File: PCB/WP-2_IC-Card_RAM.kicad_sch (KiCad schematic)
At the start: 8 parts, among them J1 Conn_01x38_Female, U1 628128_TSOP

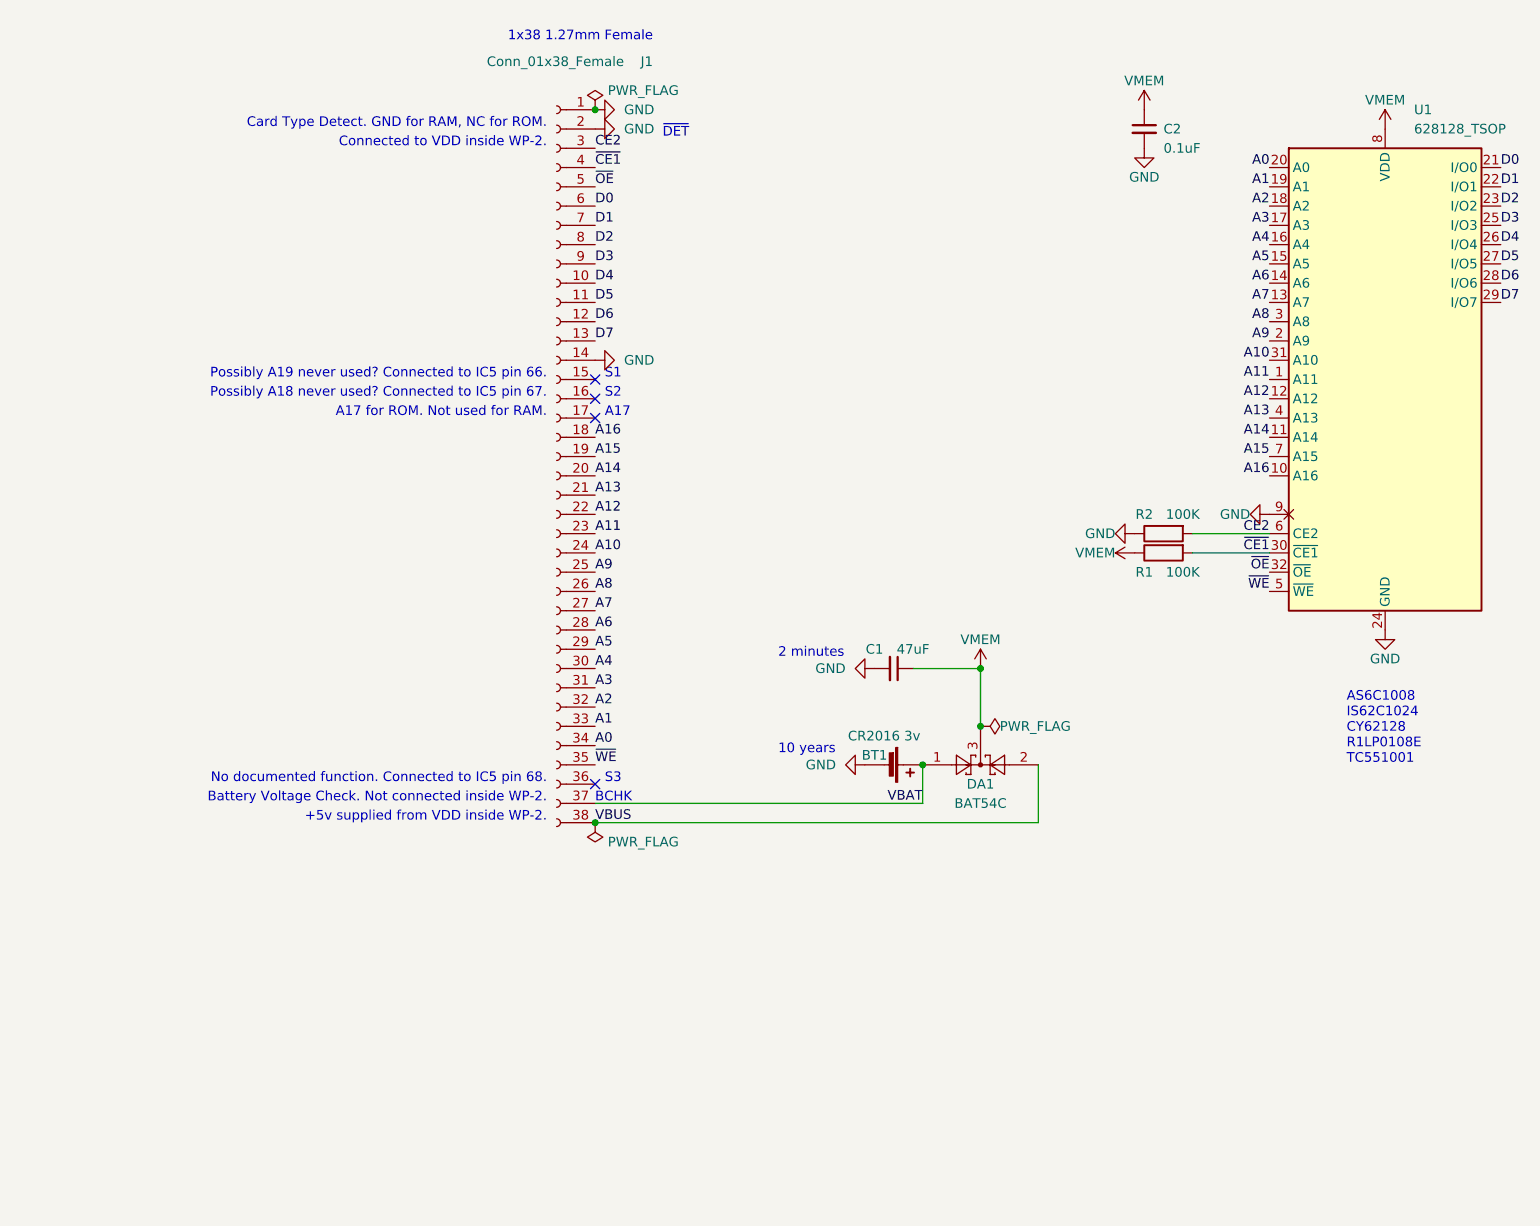
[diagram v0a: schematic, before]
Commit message: simpler caps for ram card, 3d-printed cover, new WIP 4-bank MRAM card
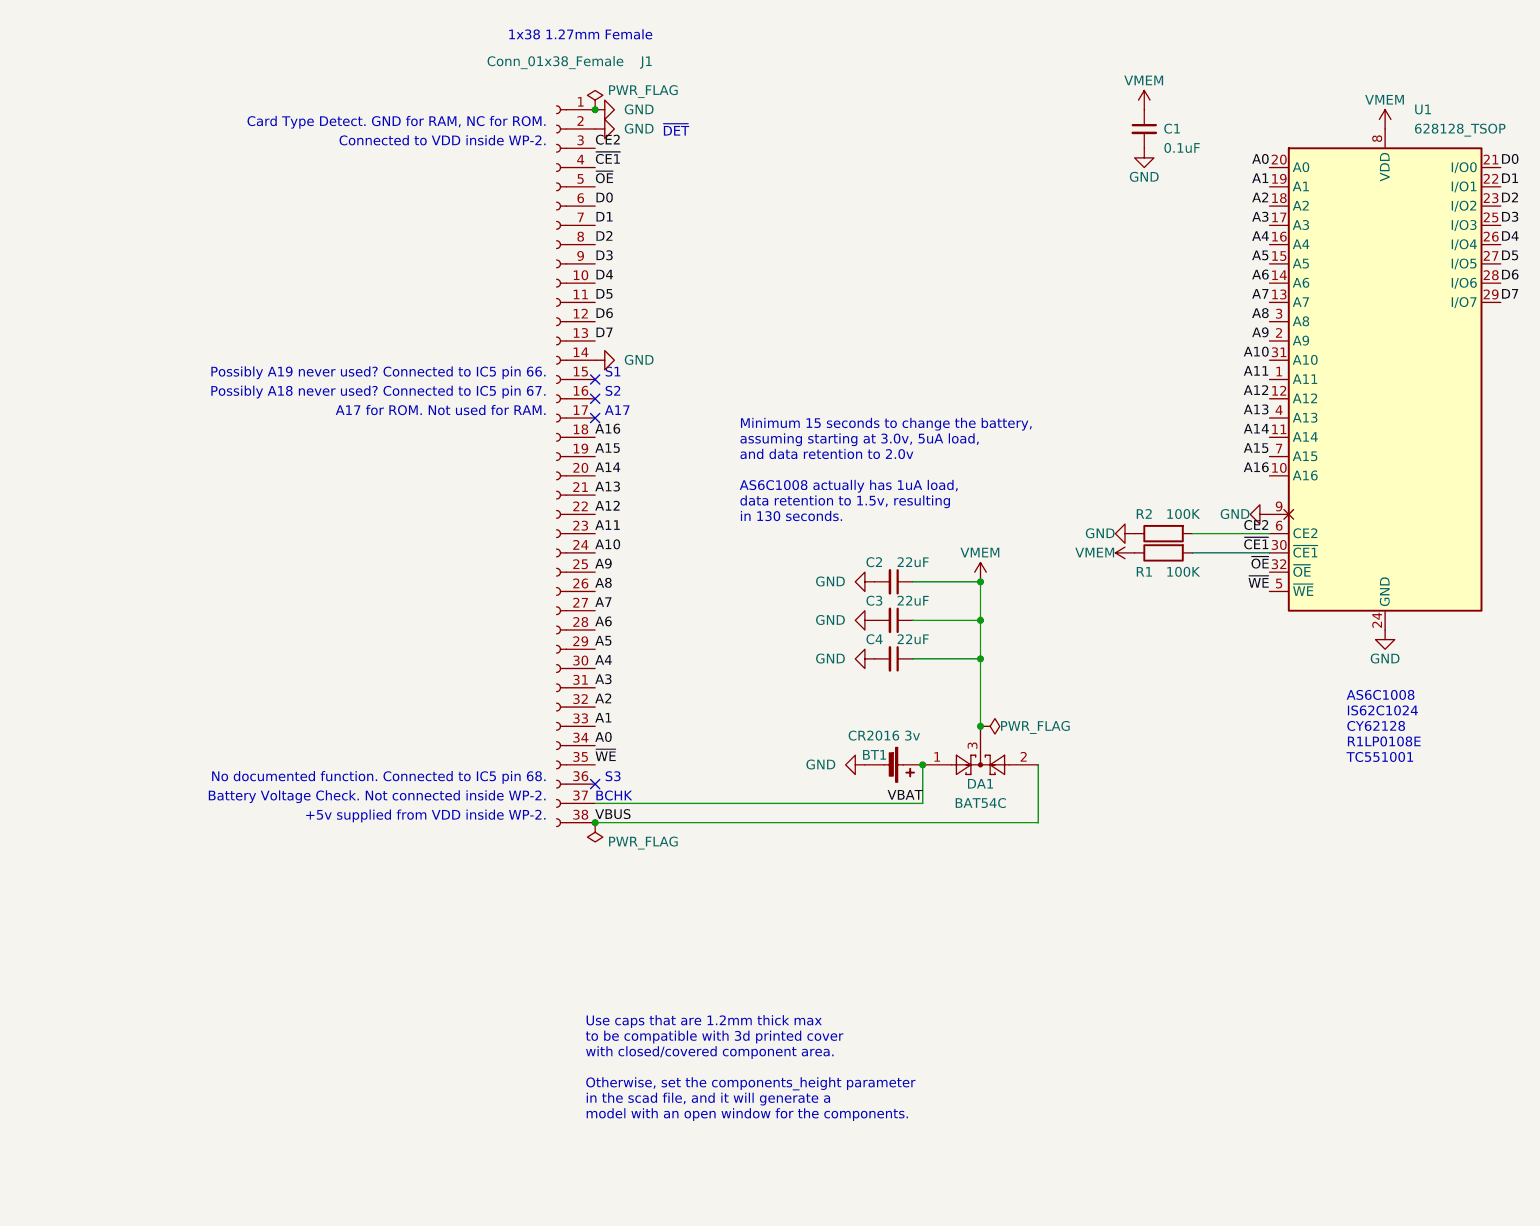
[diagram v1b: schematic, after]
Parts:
- added C3, C4: 22uF, 0_LOCAL:C_0805_1mm, symbol 0_LOCAL:C_Small
- C1: renamed from C2; footprint 0_LOCAL:C_0805 -> 0_LOCAL:C_0805_1mm
- C2: renamed from C1; value 47uF -> 22uF; footprint 0_LOCAL:C_0805 -> 0_LOCAL:C_0805_1mm
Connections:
- net GND: now also C3.2, C4.2
- net VMEM: now also C3.1, C4.1
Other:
- note added: "Minimum 15 seconds to change the battery, assuming starting at 3.0v, 5uA load, and data retention to 2.0v AS6C1008 actually has 1uA load, data retention to 1.5v, resulting in 130 seconds."
- note added: "Use caps that are 1.2mm thick max to be compatible with 3d printed cover with closed/covered component area. Otherwise, set the components_height parameter in the scad file, and it will generate a model with an open window for the components."
- note removed: "10 years"
- note removed: "2 minutes"
- moved on the sheet: C2

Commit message: readme
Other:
- note added: "Minimum 15 seconds to change the battery, assuming starting at 3.0v, 5uA load, and data retention to 2.0v AS6C1008 actually has 1uA load, data retention to 1.5v, resulting in 130 seconds. Actually tested over 10 minutes with no battery."
- note added: "The CE2 and BCHK circuits are included here even though they are no-op in the WP-2. Maybe the card might also work in other machines like the Citizen, and maybe some other machine actually uses those pins."
- note removed: "Minimum 15 seconds to change the battery, assuming starting at 3.0v, 5uA load, and data retention to 2.0v AS6C1008 actually has 1uA load, data retention to 1.5v, resulting in 130 seconds."
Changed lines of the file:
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@@
+    (effects (font (size 1.27 1.27)) (justify left bottom))
+  )
+  (text "The CE2 and BCHK circuits are included here even though they are no-op in the WP-2.\nMaybe the card might also work in other machines like the Citizen,\nand maybe some other machine actually uses those pins."
+    (at 44.45 198.12 0)
     (effects (font (size 1.27 1.27)) (justify left bottom))
   )
@@
     (effects (font (size 1.27 1.27)) (justify right bottom))
   )
-  (text "Minimum 15 seconds to change the battery,\nassuming starting at 3.0v, 5uA load,\nand data retention to 2.0v\n\nAS6C1008 actually has 1uA load,\ndata retention to 1.5v, resulting\nin 130 seconds."
-    (at 107.95 107.95 0)
+  (text "Minimum 15 seconds to change the battery,\nassuming starting at 3.0v, 5uA load,\nand data retention to 2.0v\n\nAS6C1008 actually has 1uA load,\ndata retention to 1.5v, resulting\nin 130 seconds.\n\nActually tested over 10 minutes with no battery."
+    (at 107.95 104.14 0)
     (effects (font (size 1.27 1.27)) (justify left bottom))
   )
@@
   )
   (text "Use caps that are 1.2mm thick max\nto be compatible with 3d printed cover\nwith closed/covered component area.\n\nOtherwise, set the components_height parameter\nin the scad file, and it will generate a\nmodel with an open window for the components.\n"
-    (at 87.63 186.69 0)
+    (at 44.45 185.42 0)
     (effects (font (size 1.27 1.27)) (justify left bottom))
   )

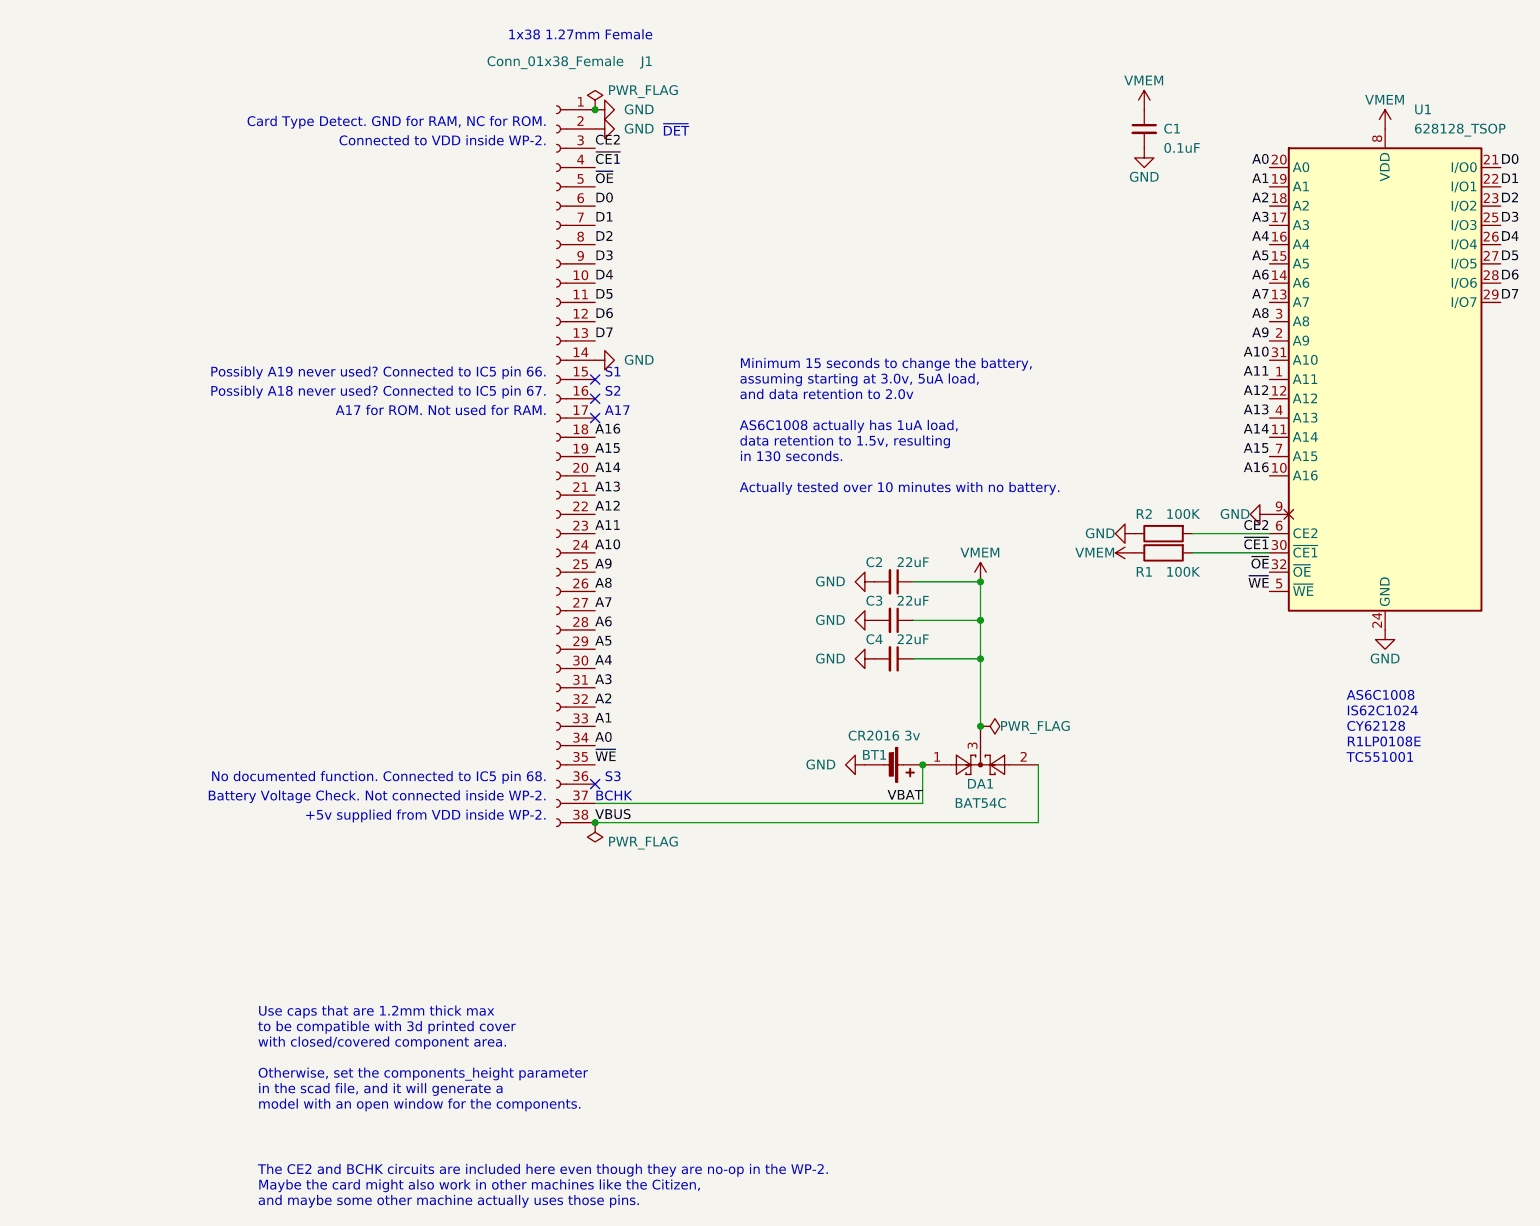
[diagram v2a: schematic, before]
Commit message: MRAM level shifters, delete FRAM, local datasheets in local symbols
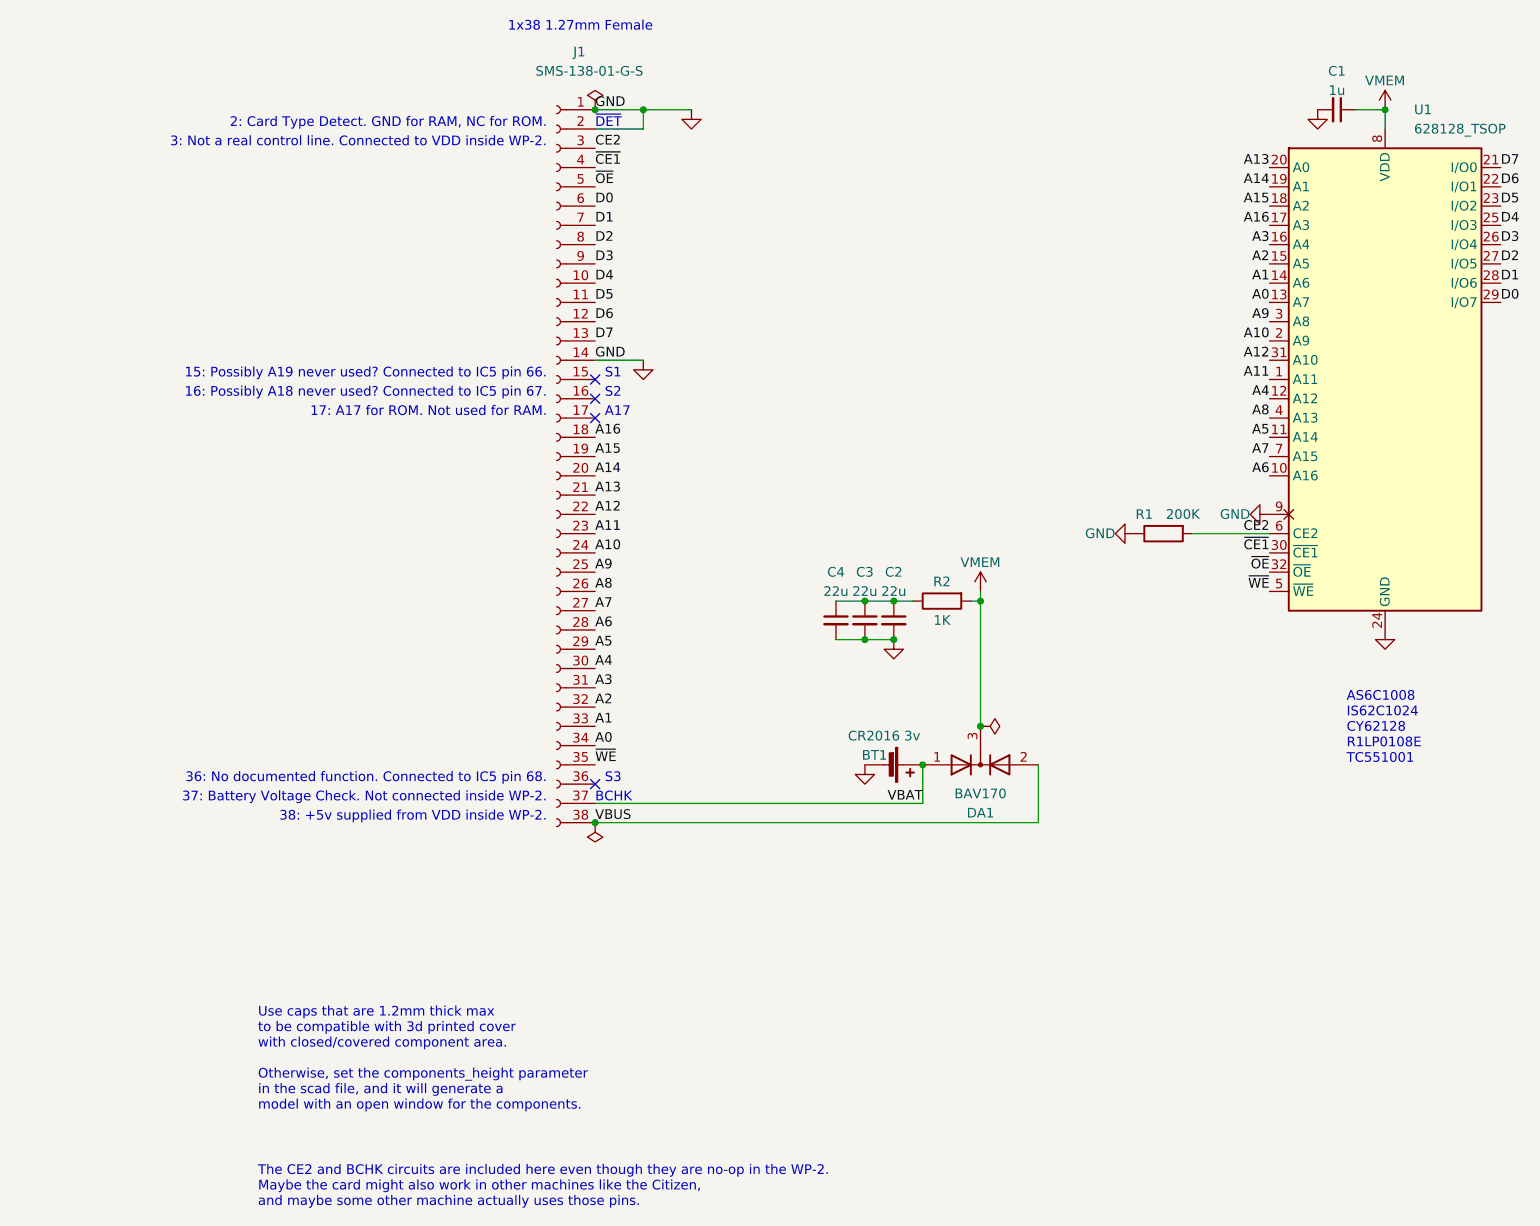
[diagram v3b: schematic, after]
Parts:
- removed DA1: BAT54C, 0_LOCAL:SOT-23, symbol 0_LOCAL:BAT54C
- added DA1: BAV170, 0_LOCAL:SOT-23, symbol 0_LOCAL:BAV170
- C1: value 0.1uF -> 1u
- C2, C3, C4: value 22uF -> 22u
- J1: value Conn_01x38_Female -> SMS-138-01-G-S
- R1: value 100K -> 200K
- R2: value 100K -> 1K
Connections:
- net A0: now also U1.13 (A7); no longer U1.20 (A0)
- net A1: now also U1.14 (A6); no longer U1.19 (A1)
- net A10: now also U1.2 (A9); no longer U1.31 (A10)
- net A12: now also U1.31 (A10); no longer U1.12 (A12)
- net A13: now also U1.20 (A0); no longer U1.4 (A13)
- net A14: now also U1.19 (A1); no longer U1.11 (A14)
- net A15: now also U1.18 (A2); no longer U1.7 (A15)
- net A16: now also U1.17 (A3); no longer U1.10 (A16)
- net A2: now also U1.15 (A5); no longer U1.18 (A2)
- net A3: now also U1.16 (A4); no longer U1.17 (A3)
- net A4: now also U1.12 (A12); no longer U1.16 (A4)
- net A5: now also U1.11 (A14); no longer U1.15 (A5)
- net A6: now also U1.10 (A16); no longer U1.14 (A6)
- net A7: now also U1.7 (A15); no longer U1.13 (A7)
- net A8: now also U1.4 (A13); no longer U1.3 (A8)
- net A9: now also U1.3 (A8); no longer U1.2 (A9)
- net CE2: now also R1.2; no longer R2.2
- net D0: now also U1.29 (I/O7); no longer U1.21 (I/O0)
- net D1: now also U1.28 (I/O6); no longer U1.22 (I/O1)
- net D2: now also U1.27 (I/O5); no longer U1.23 (I/O2)
- net D3: now also U1.26 (I/O4); no longer U1.25 (I/O3)
- net D4: now also U1.25 (I/O3); no longer U1.26 (I/O4)
- net D5: now also U1.23 (I/O2); no longer U1.27 (I/O5)
- net D6: now also U1.22 (I/O1); no longer U1.28 (I/O6)
- net D7: now also U1.21 (I/O0); no longer U1.29 (I/O7)
- net GND: now also R1.1; no longer R2.1
- net VBAT: now also DA1.1 (A)
- net VBUS: now also DA1.2 (A)
- net VMEM: now also R2.2, DA1.3 (K); no longer C2.1, C3.1, C4.1, R1.1
- net ~{CE1}: no longer R1.2
- new net: C2.1, C3.1, C4.1, R2.1
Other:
- note added: "15: Possibly A19 never used? Connected to IC5 pin 66."
- note added: "16: Possibly A18 never used? Connected to IC5 pin 67."
- note added: "17: A17 for ROM. Not used for RAM."
- note added: "2: Card Type Detect. GND for RAM, NC for ROM."
- note added: "36: No documented function. Connected to IC5 pin 68."
- note added: "37: Battery Voltage Check. Not connected inside WP-2."
- note added: "38: +5v supplied from VDD inside WP-2."
- note added: "3: Not a real control line. Connected to VDD inside WP-2."
- note removed: "+5v supplied from VDD inside WP-2."
- note removed: "A17 for ROM. Not used for RAM."
- note removed: "Battery Voltage Check. Not connected inside WP-2."
- note removed: "Card Type Detect. GND for RAM, NC for ROM."
- note removed: "Connected to VDD inside WP-2."
- note removed: "Minimum 15 seconds to change the battery, assuming starting at 3.0v, 5uA load, and data retention to 2.0v AS6C1008 actually has 1uA load, data retention to 1.5v, resulting in 130 seconds. Actually tested over 10 minutes with no battery."
- note removed: "No documented function. Connected to IC5 pin 68."
- note removed: "Possibly A18 never used? Connected to IC5 pin 67."
- note removed: "Possibly A19 never used? Connected to IC5 pin 66."
- moved on the sheet: C2, R1

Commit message: ram 128 move vias off pads and add MPN and fab_bom.csv
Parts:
- BT1: MPN (none) -> Keystone 3026
- C1: MPN (none) -> CL21A105KBCLNNC
- C2, C3, C4: MPN (none) -> CL21A226MOCLRNC
- DA1: MPN (none) -> BAV170-7-F
- J1: MPN (none) -> SMS-138-01-G-S
- R1: MPN (none) -> CRCW0805200KFKEA
- R2: MPN (none) -> CRCW08051K00FKEA
- U1: MPN (none) -> AS6C1008-55STIN
